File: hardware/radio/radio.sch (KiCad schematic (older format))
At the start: 4 parts, among them P101 CONN_01X04, P102 CONN_02X03, P103 CONN_02X05, P104 CONN_01X02

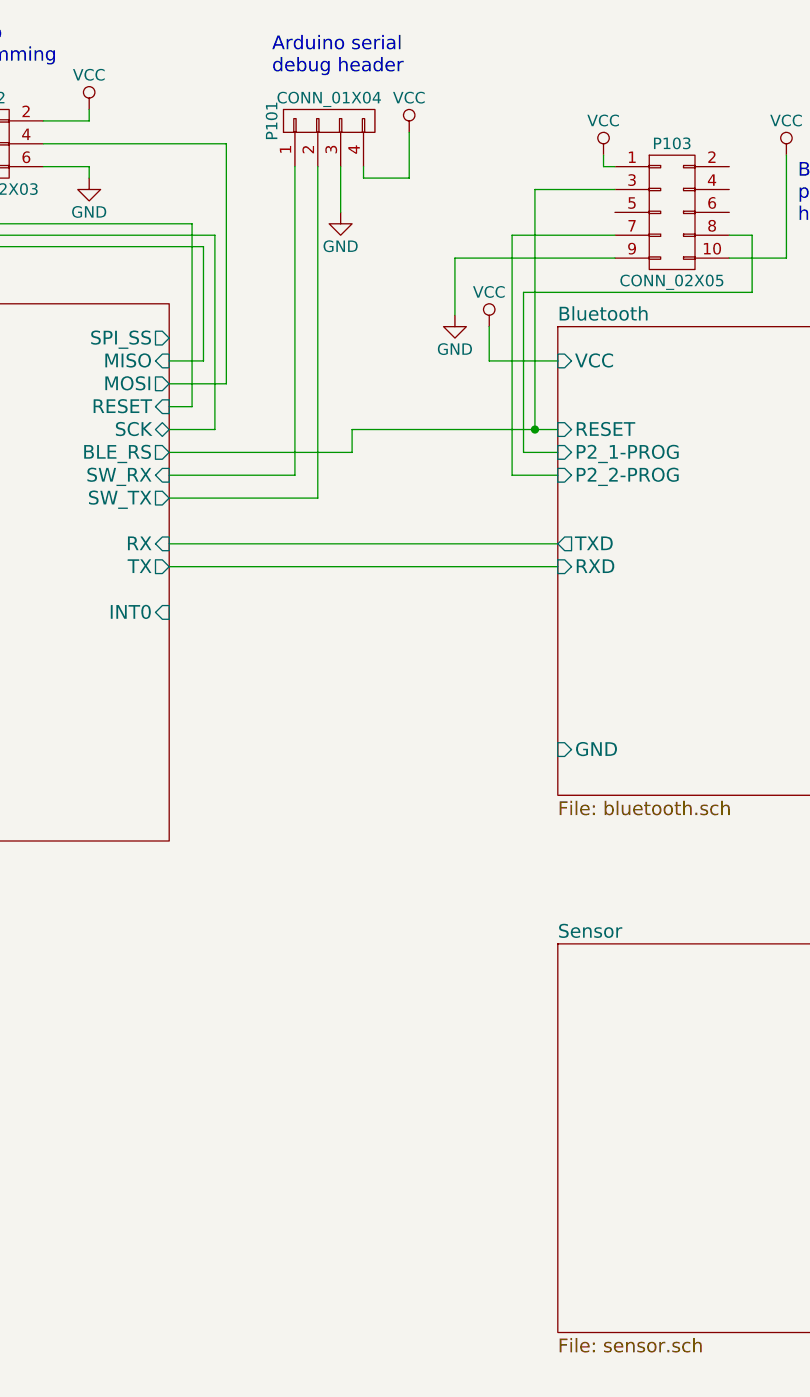
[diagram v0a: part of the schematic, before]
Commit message: Add accelerometer to schematic
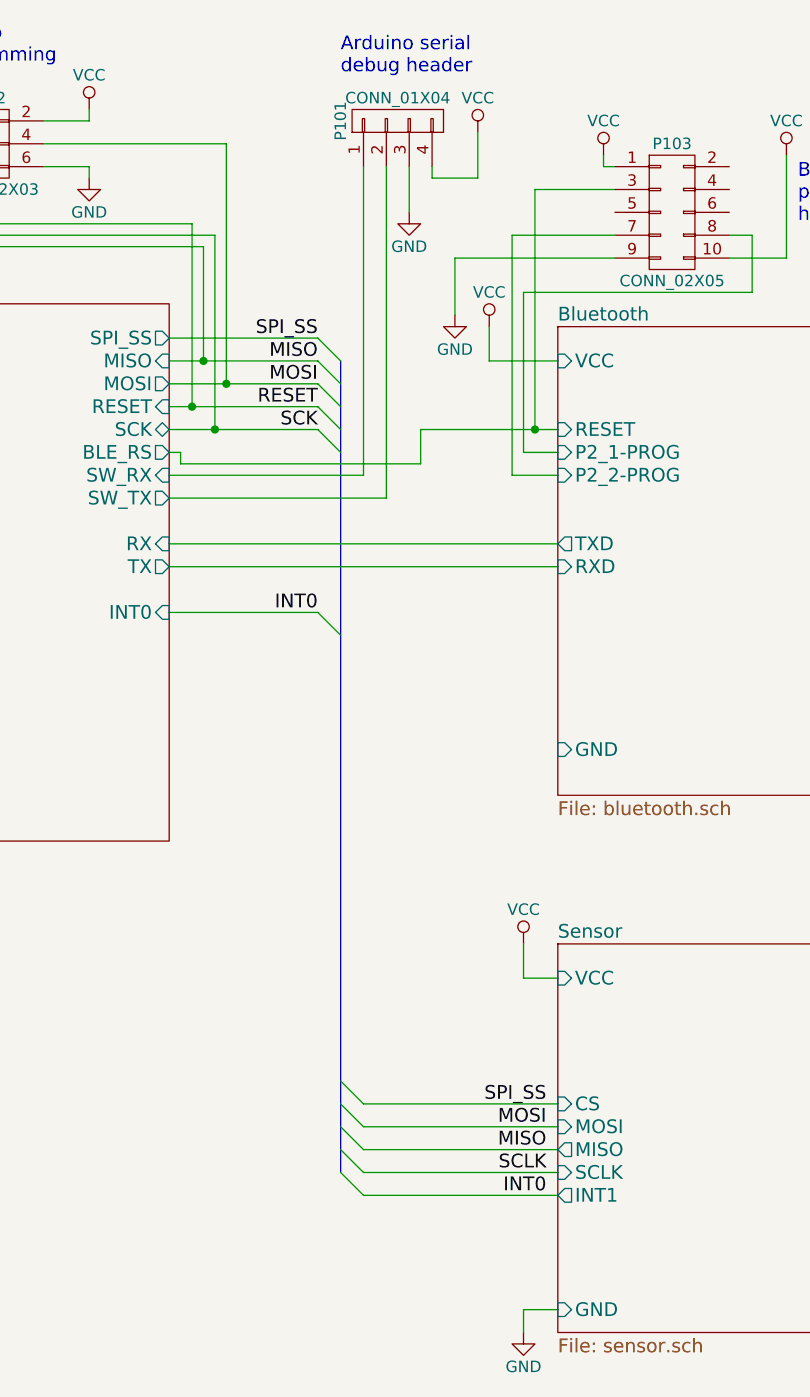
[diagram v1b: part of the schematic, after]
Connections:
- net Control/MISO renamed MISO
- net Control/MOSI renamed MOSI
- net Control/RESET renamed RESET
- net Control/SCK renamed SCK
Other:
- moved on the sheet: P101
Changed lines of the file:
@@
 LIBS:sensors
 LIBS:rfcom
+LIBS:radio-cache
 EELAYER 25 0
 EELAYER END
@@
 F0 "Sensor" 60
 F1 "sensor.sch" 60
+F2 "CS" I L 8050 5250 60
+F3 "MOSI" I L 8050 5350 60
+F4 "MISO" O L 8050 5450 60
+F5 "SCLK" I L 8050 5550 60
+F6 "INT1" O L 8050 5650 60
+F7 "VCC" I L 8050 4700 60
+F8 "GND" I L 8050 6150 60
 $EndSheet
 Wire Wire Line
@@
 	4500 3950 4500 4200
 $Comp
-L GND #PWR01
+L GND #PWR111
 U 1 1 55EB4CC6
 P 4500 4200
-F 0 "#PWR01" H 4500 3950 50  0001 C CNN
+F 0 "#PWR111" H 4500 3950 50  0001 C CNN
 F 1 "GND" H 4500 4050 50  0000 C CNN
 F 2 "" H 4500 4200 60  0000 C CNN
@@
 $EndComp
 $Comp
-L GND #PWR02
+L GND #PWR110
 U 1 1 55EB4D76
 P 2900 4200
-F 0 "#PWR02" H 2900 3950 50  0001 C CNN
+F 0 "#PWR110" H 2900 3950 50  0001 C CNN
 F 1 "GND" H 2900 4050 50  0000 C CNN
 F 2 "" H 2900 4200 60  0000 C CNN
@@
 	8050 2900 6350 2900
 Wire Wire Line
-	6350 2400 7150 2400
-Wire Wire Line
-	7150 2400 7150 2300
-Wire Wire Line
-	7150 2300 8050 2300
+	7450 2300 7450 2450
+Wire Wire Line
+	7450 2300 8050 2300
 $Comp
 L CONN_01X02 P104
@@
 	1000 2150 1300 2150
 $Comp
-L PWR_FLAG #FLG03
+L PWR_FLAG #FLG101
 U 1 1 55EBB1ED
 P 1000 1400
-F 0 "#FLG03" H 1000 1495 50  0001 C CNN
+F 0 "#FLG101" H 1000 1495 50  0001 C CNN
 F 1 "PWR_FLAG" H 1000 1580 50  0000 C CNN
 F 2 "" H 1000 1400 60  0000 C CNN
@@
 $EndComp
 $Comp
-L PWR_FLAG #FLG04
+L PWR_FLAG #FLG102
 U 1 1 55EBB2CF
 P 1200 1700
-F 0 "#FLG04" H 1200 1795 50  0001 C CNN
+F 0 "#FLG102" H 1200 1795 50  0001 C CNN
 F 1 "PWR_FLAG" H 1200 1880 50  0000 C CNN
 F 2 "" H 1200 1700 60  0000 C CNN
@@
 	8250 1150 8250 1100
 $Comp
-L VCC #PWR05
+L VCC #PWR104
 U 1 1 55EBE042
 P 9050 1100
-F 0 "#PWR05" H 9050 950 50  0001 C CNN
+F 0 "#PWR104" H 9050 950 50  0001 C CNN
 F 1 "VCC" H 9050 1250 50  0000 C CNN
 F 2 "" H 9050 1100 60  0000 C CNN
@@
 $EndComp
 $Comp
-L VCC #PWR06
+L VCC #PWR103
 U 1 1 55EBE126
 P 8250 1100
-F 0 "#PWR06" H 8250 950 50  0001 C CNN
+F 0 "#PWR103" H 8250 950 50  0001 C CNN
 F 1 "VCC" H 8250 1250 50  0000 C CNN
 F 2 "" H 8250 1100 60  0000 C CNN
@@
 $EndComp
 $Comp
-L GND #PWR07
+L GND #PWR108
 U 1 1 55EBE5B7
 P 7600 1800
-F 0 "#PWR07" H 7600 1550 50  0001 C CNN
+F 0 "#PWR108" H 7600 1550 50  0001 C CNN
 F 1 "GND" H 7600 1650 50  0000 C CNN
 F 2 "" H 7600 1800 60  0000 C CNN
@@
 $EndComp
 $Comp
-L VCC #PWR08
+L VCC #PWR109
 U 1 1 55EBE69B
 P 7750 1850
-F 0 "#PWR08" H 7750 1700 50  0001 C CNN
+F 0 "#PWR109" H 7750 1700 50  0001 C CNN
 F 1 "VCC" H 7750 2000 50  0000 C CNN
 F 2 "" H 7750 1850 60  0000 C CNN
@@
 BLE113\nprogramming\nheader
 $Comp
-L VCC #PWR09
+L VCC #PWR107
 U 1 1 55EC0D57
 P 3750 1800
-F 0 "#PWR09" H 3750 1650 50  0001 C CNN
+F 0 "#PWR107" H 3750 1650 50  0001 C CNN
 F 1 "VCC" H 3750 1950 50  0000 C CNN
 F 2 "" H 3750 1800 60  0000 C CNN
@@
 $EndComp
 Wire Wire Line
-	6350 2300 6550 2300
+	6350 2300 7000 2300
 Wire Wire Line
 	6550 2300 6550 1450
@@
 	5100 1050 5300 1050
 Wire Wire Line
-	6350 2000 6500 2000
+	6350 2000 7000 2000
 Wire Wire Line
 	6500 2000 6500 1500
@@
 	5050 950  5300 950
 Wire Wire Line
-	6350 2100 6600 2100
+	6350 2100 7000 2100
 Wire Wire Line
 	6600 2100 6600 1050
@@
 	6000 1150 6000 1200
 Wire Wire Line
-	6350 2200 6450 2200
+	6350 2200 7000 2200
 Wire Wire Line
 	6450 2200 6450 1400
@@
 	5200 1150 5300 1150
 $Comp
-L VCC #PWR010
+L VCC #PWR101
 U 1 1 55EC31B4
 P 6000 900
-F 0 "#PWR010" H 6000 750 50  0001 C CNN
+F 0 "#PWR101" H 6000 750 50  0001 C CNN
 F 1 "VCC" H 6000 1050 50  0000 C CNN
 F 2 "" H 6000 900 60  0000 C CNN
@@
 $EndComp
 $Comp
-L GND #PWR011
+L GND #PWR105
 U 1 1 55EC336C
 P 6000 1200
-F 0 "#PWR011" H 6000 950 50  0001 C CNN
+F 0 "#PWR105" H 6000 950 50  0001 C CNN
 F 1 "GND" H 6000 1050 50  0000 C CNN
 F 2 "" H 6000 1200 60  0000 C CNN
@@
 L CONN_01X04 P101
 U 1 1 55EC3C1E
-P 7050 950
-F 0 "P101" H 7050 1200 50  0000 C CNN
-F 1 "CONN_01X04" V 7150 950 50  0000 C CNN
-F 2 "" H 7050 950 60  0000 C CNN
-F 3 "" H 7050 950 60  0000 C CNN
-	1    7050 950
+P 7350 950
+F 0 "P101" H 7350 1200 50  0000 C CNN
+F 1 "CONN_01X04" V 7450 950 50  0000 C CNN
+F 2 "" H 7350 950 60  0000 C CNN
+F 3 "" H 7350 950 60  0000 C CNN
+	1    7350 950
 	0    -1   -1   0
 $EndComp
 Wire Wire Line
-	6350 2500 6900 2500
-Wire Wire Line
-	6900 2500 6900 1150
-Wire Wire Line
-	6350 2600 7000 2600
-Wire Wire Line
-	7000 2600 7000 1150
-Wire Wire Line
-	7200 1150 7200 1200
-Wire Wire Line
-	7200 1200 7400 1200
-Wire Wire Line
-	7400 1200 7400 1000
-Wire Wire Line
-	7100 1150 7100 1350
-$Comp
-L GND #PWR012
+	6350 2500 7200 2500
+Wire Wire Line
+	7200 2500 7200 1150
+Wire Wire Line
+	6350 2600 7300 2600
+Wire Wire Line
+	7300 2600 7300 1150
+Wire Wire Line
+	7500 1150 7500 1200
+Wire Wire Line
+	7500 1200 7700 1200
+Wire Wire Line
+	7700 1200 7700 1000
+Wire Wire Line
+	7400 1150 7400 1350
+$Comp
+L GND #PWR106
 U 1 1 55EC4334
-P 7100 1350
-F 0 "#PWR012" H 7100 1100 50  0001 C CNN
-F 1 "GND" H 7100 1200 50  0000 C CNN
-F 2 "" H 7100 1350 60  0000 C CNN
-F 3 "" H 7100 1350 60  0000 C CNN
-	1    7100 1350
-	1    0    0    -1
-$EndComp
-$Comp
-L VCC #PWR013
+P 7400 1350
+F 0 "#PWR106" H 7400 1100 50  0001 C CNN
+F 1 "GND" H 7400 1200 50  0000 C CNN
+F 2 "" H 7400 1350 60  0000 C CNN
+F 3 "" H 7400 1350 60  0000 C CNN
+	1    7400 1350
+	1    0    0    -1
+$EndComp
+$Comp
+L VCC #PWR102
 U 1 1 55EC45C4
-P 7400 1000
-F 0 "#PWR013" H 7400 850 50  0001 C CNN
-F 1 "VCC" H 7400 1150 50  0000 C CNN
-F 2 "" H 7400 1000 60  0000 C CNN
-F 3 "" H 7400 1000 60  0000 C CNN
-	1    7400 1000
-	1    0    0    -1
-$EndComp
-Text Notes 6800 750  0    60   ~ 0
+P 7700 1000
+F 0 "#PWR102" H 7700 850 50  0001 C CNN
+F 1 "VCC" H 7700 1150 50  0000 C CNN
+F 2 "" H 7700 1000 60  0000 C CNN
+F 3 "" H 7700 1000 60  0000 C CNN
+	1    7700 1000
+	1    0    0    -1
+$EndComp
+Text Notes 7100 750  0    60   ~ 0
 Arduino serial \ndebug header
+Wire Bus Line
+	7100 2000 7100 5550
+Entry Wire Line
+	7000 1900 7100 2000
+Entry Wire Line
+	7000 2000 7100 2100
+Entry Wire Line
+	7000 2100 7100 2200
+Entry Wire Line
+	7000 2200 7100 2300
+Entry Wire Line
+	7000 2300 7100 2400
+Wire Wire Line
+	6350 2400 6400 2400
+Wire Wire Line
+	6400 2400 6400 2450
+Wire Wire Line
+	6400 2450 7450 2450
+Wire Wire Line
+	7000 1900 6350 1900
+Connection ~ 6500 2000
+Connection ~ 6600 2100
+Connection ~ 6450 2200
+Connection ~ 6550 2300
+Text Label 7000 1900 2    60   ~ 0
+SPI_SS
+Text Label 7000 2000 2    60   ~ 0
+MISO
+Text Label 7000 2100 2    60   ~ 0
+MOSI
+Text Label 7000 2200 2    60   ~ 0
+RESET
+Text Label 7000 2300 2    60   ~ 0
+SCK
+Wire Wire Line
+	6350 3100 7000 3100
+Entry Wire Line
+	7000 3100 7100 3200
+Text Label 7000 3100 2    60   ~ 0
+INT0
+Entry Wire Line
+	7100 5550 7200 5650
+Entry Wire Line
+	7100 5450 7200 5550
+Entry Wire Line
+	7100 5350 7200 5450
+Entry Wire Line
+	7100 5250 7200 5350
+Entry Wire Line
+	7100 5150 7200 5250
+Wire Wire Line
+	8050 5250 7200 5250
+Wire Wire Line
+	7200 5350 8050 5350
+Wire Wire Line
+	8050 5450 7200 5450
+Wire Wire Line
+	7200 5550 8050 5550
+Wire Wire Line
+	8050 5650 7200 5650
+Text Label 8000 5650 2    60   ~ 0
+INT0
+Text Label 8000 5550 2    60   ~ 0
+SCLK
+Text Label 8000 5450 2    60   ~ 0
+MISO
+Text Label 8000 5350 2    60   ~ 0
+MOSI
+Text Label 8000 5250 2    60   ~ 0
+SPI_SS
+Wire Wire Line
+	8050 4700 7900 4700
+Wire Wire Line
+	7900 4700 7900 4550
+Wire Wire Line
+	8050 6150 7900 6150
+Wire Wire Line
+	7900 6150 7900 6250
+$Comp
+L GND #PWR113
+U 1 1 55ECE90B
+P 7900 6250
+F 0 "#PWR113" H 7900 6000 50  0001 C CNN
+F 1 "GND" H 7900 6100 50  0000 C CNN
+F 2 "" H 7900 6250 60  0000 C CNN
+F 3 "" H 7900 6250 60  0000 C CNN
+	1    7900 6250
+	1    0    0    -1
+$EndComp
+$Comp
+L VCC #PWR112
+U 1 1 55ECEA1D
+P 7900 4550
+F 0 "#PWR112" H 7900 4400 50  0001 C CNN
+F 1 "VCC" H 7900 4700 50  0000 C CNN
+F 2 "" H 7900 4550 60  0000 C CNN
+F 3 "" H 7900 4550 60  0000 C CNN
+	1    7900 4550
+	1    0    0    -1
+$EndComp
 $EndSCHEMATC
